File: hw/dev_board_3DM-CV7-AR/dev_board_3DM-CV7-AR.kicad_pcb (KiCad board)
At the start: 2 copper layers, 66.5 x 35 mm, 11 parts

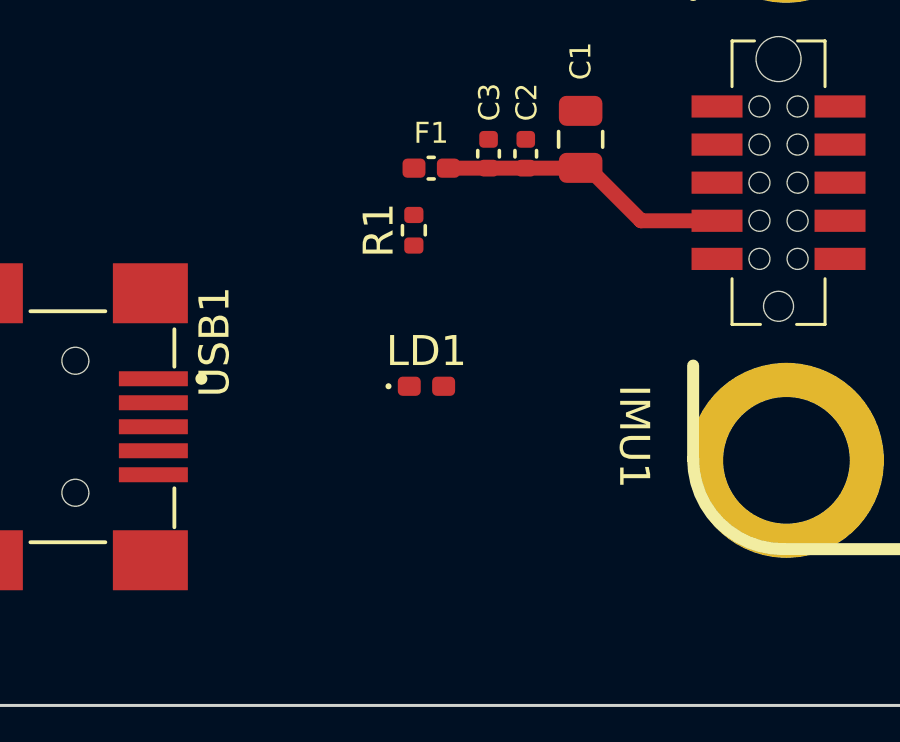
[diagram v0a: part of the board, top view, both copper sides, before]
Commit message: Añadido CM Choke
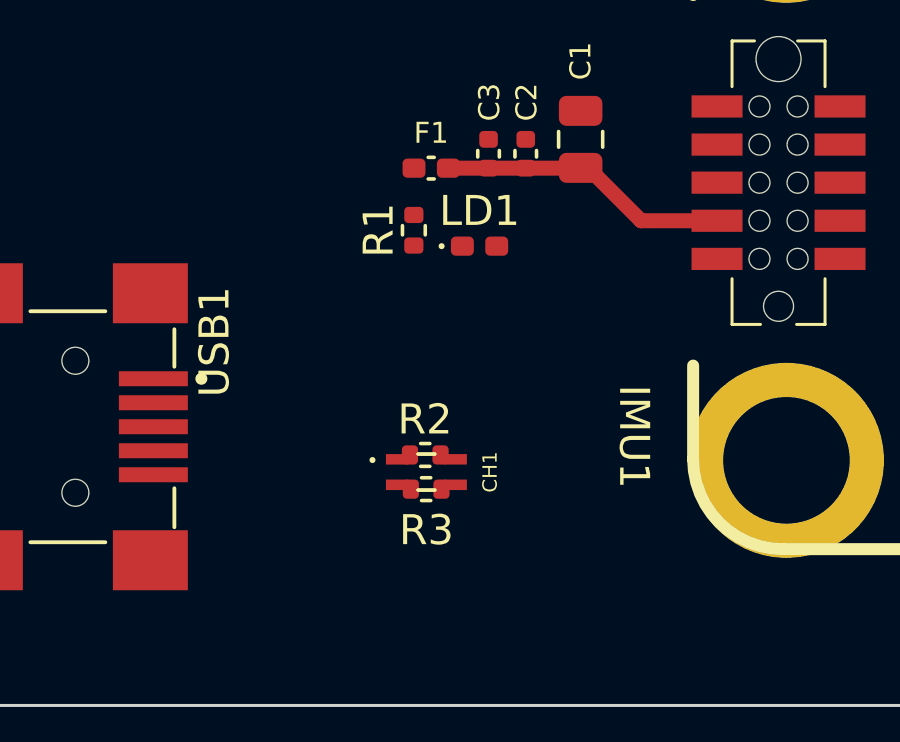
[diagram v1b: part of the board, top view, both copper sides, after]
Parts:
- added CH1: ~, Herranz - Filtering:XFMR_CM0805D900R-10, F.Cu at (111.0, 106.9)
- added R2: 0, Resistor_SMD:R_0402_1005Metric, F.Cu at (111.0, 106.4)
- added R3: 0, Resistor_SMD:R_0402_1005Metric, F.Cu at (111.0, 107.5)
- moved LD1 4.99 mm to (112.8, 99.4)
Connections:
- IMU1 pad 1: unconnected-(IMU1-USB_D--Pad1) -> Net-(IMU1-USB_D-)
- IMU1 pad 2: unconnected-(IMU1-USB_D+-Pad2) -> Net-(IMU1-USB_D+)
- USB1 pad 2: unconnected-(USB1-D--Pad2) -> Net-(USB1-D-)
- USB1 pad 3: unconnected-(USB1-D+-Pad3) -> Net-(USB1-D+)

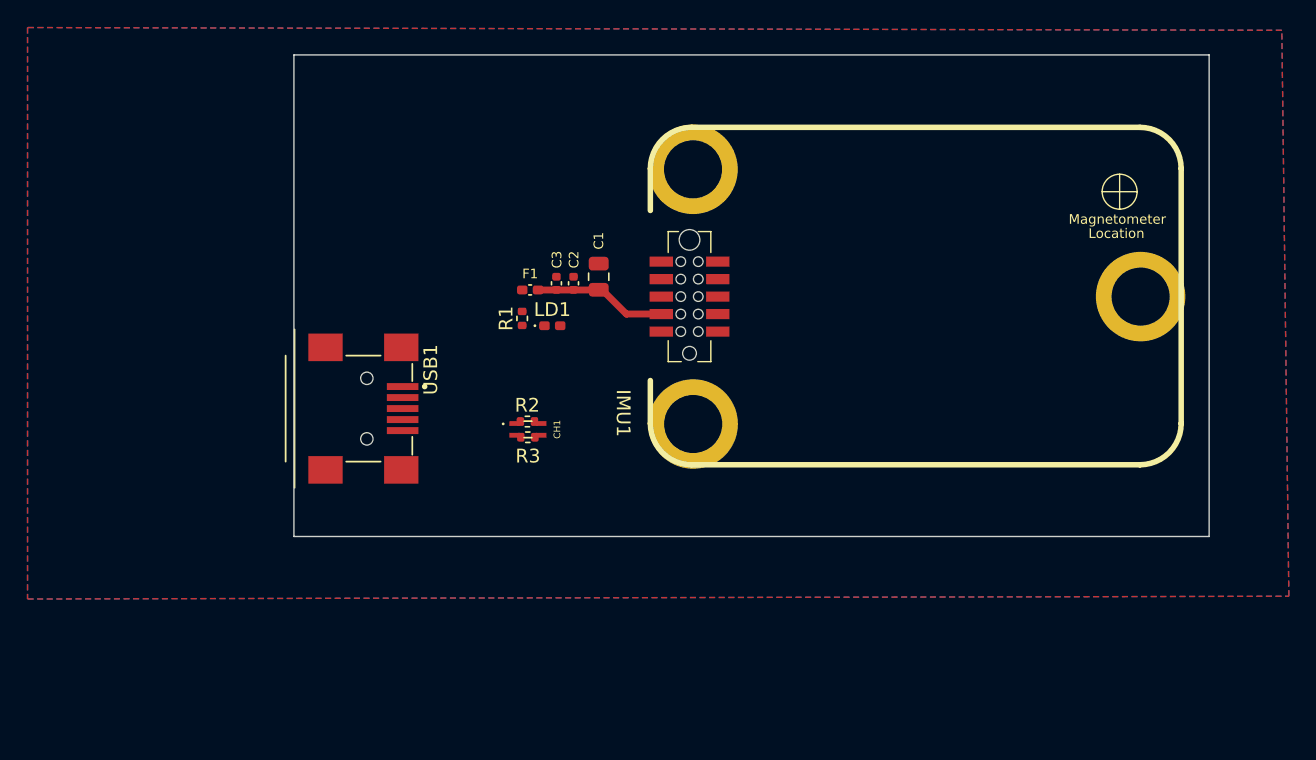
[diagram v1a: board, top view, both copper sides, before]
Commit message: Añadido Leds TX-RX
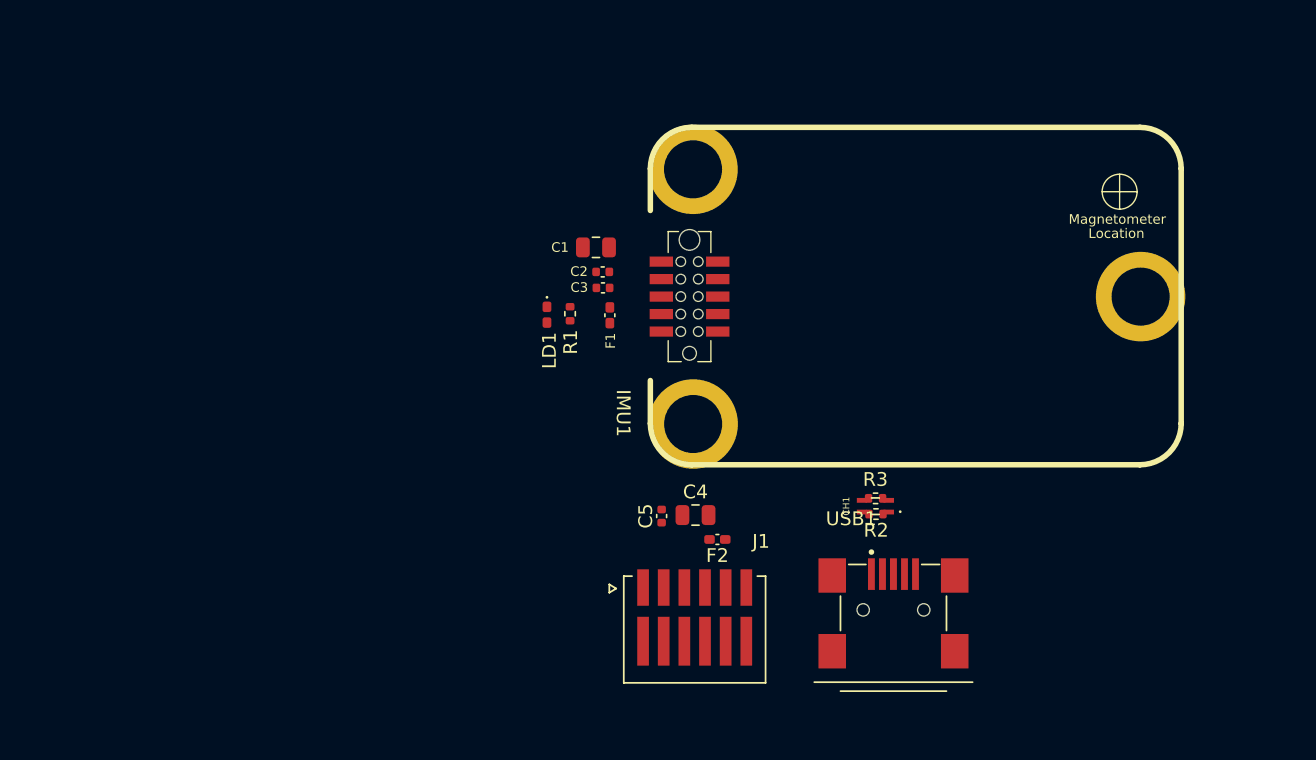
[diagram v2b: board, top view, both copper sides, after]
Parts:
- added C4: 0.1uF, Capacitor_SMD:C_0805_2012Metric, F.Cu at (123.2, 113.2)
- added C5: 0.1uF, Capacitor_SMD:C_0402_1005Metric, F.Cu at (120.7, 113.2)
- added F2: ~, Inductor_SMD:L_0402_1005Metric_Pad0.77x0.64mm_HandSolder, F.Cu at (124.8, 114.9)
- added J1: 87438-0643, Herranz - Conn Molex:Molex_picoSPOX_87438-3.5A_1x6_P1.5mm_Horizontal, F.Cu at (123.2, 113.2)
- moved USB1 37.8 mm to (137.6, 117.6), turned to 0 degrees
- moved R2 26.2 mm to (136.3, 113.1), turned to 180 degrees
- moved CH1 25.8 mm to (136.2, 112.5), turned to 180 degrees
- moved R3 25.6 mm to (136.2, 112.0), turned to 180 degrees
- moved F1 6.08 mm to (117.0, 98.7), turned to 90 degrees
- moved R1 3.50 mm to (114.1, 98.5), turned to -90 degrees
- moved C3 3.40 mm to (116.5, 96.7), turned to 180 degrees
- moved C2 2.28 mm to (116.4, 95.5), turned to 180 degrees
- moved C1 2.14 mm to (115.9, 93.7), turned to 180 degrees
- moved LD1 0.89 mm to (112.4, 98.6), turned to -90 degrees
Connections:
- IMU1 pad 4: unconnected-(IMU1-RxD-Pad4) -> /Rx
- IMU1 pad 5: unconnected-(IMU1-TxD-Pad5) -> /Tx
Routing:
- net Net-(IMU1-VCC): track 9.69 -> 0.00 mm
- removed copper zone on B.Cu, net GND
- removed copper zone on F.Cu, net GND
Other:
- board outline removed

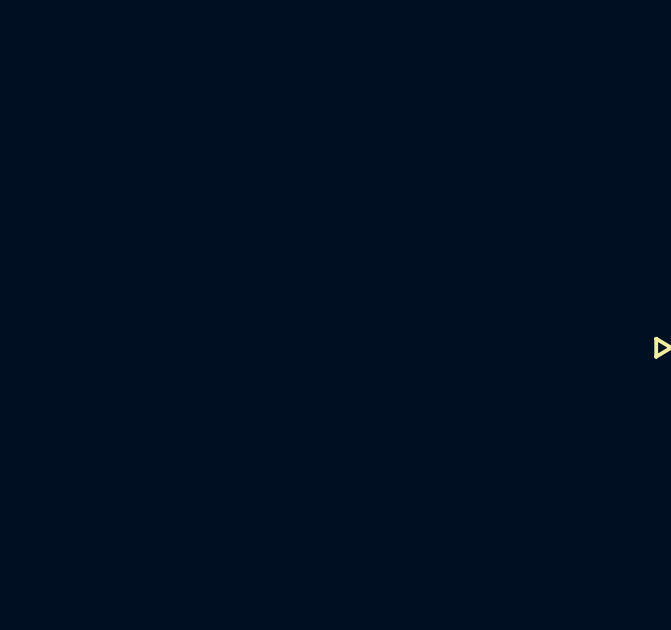
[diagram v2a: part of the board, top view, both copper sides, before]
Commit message: arreglado linea diferencial
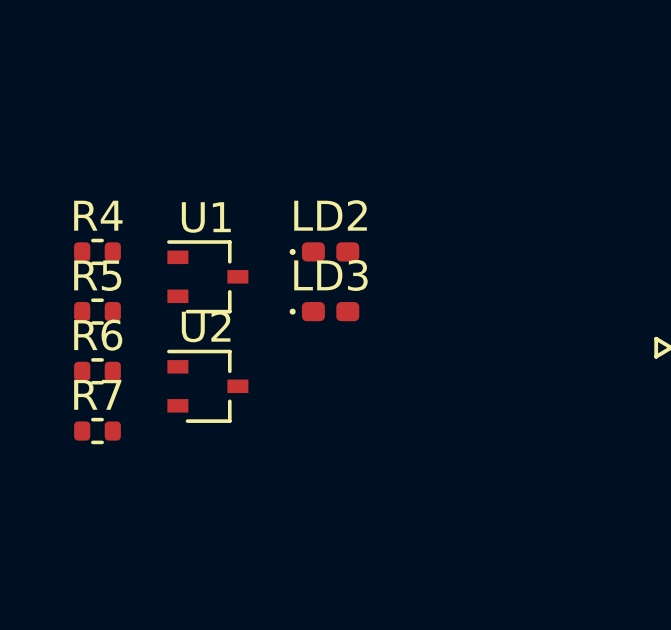
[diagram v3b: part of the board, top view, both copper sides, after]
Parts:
- added LD2: LED_Generic, LED_SMD:LED_0402_1005Metric_Pad0.77x0.64mm_HandSolder, F.Cu at (106.1, 115.3)
- added LD3: LED_Generic, LED_SMD:LED_0402_1005Metric_Pad0.77x0.64mm_HandSolder, F.Cu at (106.1, 117.3)
- added R4: 0, Resistor_SMD:R_0402_1005Metric, F.Cu at (98.3, 115.3)
- added R5: 0, Resistor_SMD:R_0402_1005Metric, F.Cu at (98.3, 117.3)
- added R6: 1.0K, Resistor_SMD:R_0402_1005Metric, F.Cu at (98.3, 119.3)
- added R7: 1.0K, Resistor_SMD:R_0402_1005Metric, F.Cu at (98.3, 121.3)
- added U1: DMP2240UW, Package_TO_SOT_SMD:SOT-323_SC-70, F.Cu at (102.0, 116.1)
- added U2: DMP2240UW, Package_TO_SOT_SMD:SOT-323_SC-70, F.Cu at (102.0, 119.8)
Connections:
- net Net-(IMU1-USB_D+) renamed /D+
- net Net-(IMU1-USB_D-) renamed /D-
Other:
- copper layers 2 -> 4

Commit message: Finalizado
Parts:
- added MC4: M3_Hole, Herranz - Various:M3_Hole, F.Cu at (157.4, 122.0)
- added MC5: M3_Hole, Herranz - Various:M3_Hole, F.Cu at (114.4, 86.7)
- added MC6: M3_Hole, Herranz - Various:M3_Hole, F.Cu at (114.4, 122.0)
- added SEL1: ~, Herranz - Various:pad_selector, F.Cu at (120.3, 113.2)
- moved R6 18.9 mm to (113.3, 107.8)
- moved R7 17.7 mm to (113.1, 111.7)
- moved R5 17.6 mm to (115.7, 115.2), turned to 180 degrees
- moved R4 16.0 mm to (113.3, 109.8)
- moved U1 15.7 mm to (115.9, 108.8), turned to 90 degrees
- moved U2 15.6 mm to (115.9, 112.7), turned to 90 degrees
- moved LD2 11.6 mm to (113.4, 106.3)
- moved LD3 8.12 mm to (113.2, 113.4)
- moved C4 2.78 mm to (125.9, 113.2)
- moved C5 2.78 mm to (123.5, 113.2)
- moved F2 2.78 mm to (127.5, 114.9)
- moved J1 2.78 mm to (125.9, 113.2)
- moved USB1 1.95 mm to (139.5, 117.6)
- moved CH1 1.95 mm to (138.2, 112.5)
- moved R2 1.95 mm to (138.2, 113.0)
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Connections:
- net Net-(USB1-D+) renamed /D_conn+
- net Net-(USB1-D-) renamed /D_conn-
- F1 pad 1: +3V3 -> +5VD
- MC3 pad 1: GND -> unconnected-(MC3-Pad1)
- R1 pad 2: +3V3 -> +5VD
- R6 pad 2: Net-(U1-S) -> Net-(U1-D)
- R7 pad 2: Net-(U2-S) -> Net-(U2-D)
- U1 pad 2: Net-(U1-S) -> +5VD
- U1 pad 3: +3V3 -> Net-(U1-D)
- U2 pad 2: Net-(U2-S) -> +5VD
- U2 pad 3: +3V3 -> Net-(U2-D)
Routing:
- net /Rx: track 0.00 -> 48.2 mm, vias 0 -> 2
- net /Tx: track 0.00 -> 35.9 mm, vias 0 -> 3
- net /D-: track 0.00 -> 24.0 mm
- net +5VD: track 0.00 -> 22.0 mm
- net VBUS: track 0.00 -> 21.0 mm
- net /D+: track 0.00 -> 19.3 mm
- net +5V: track 0.00 -> 8.59 mm
- net Net-(IMU1-VCC): track 0.00 -> 8.32 mm
- net /D_conn+: track 0.00 -> 7.97 mm
- net /D_conn-: track 0.00 -> 7.31 mm
- net Net-(J1-Pin_5): track 0.00 -> 3.50 mm
- net Net-(U2-D): track 0.00 -> 2.23 mm
- net Net-(U1-D): track 0.00 -> 2.06 mm
- net Net-(LD3-A): track 0.00 -> 1.75 mm
- net Net-(LD1-A): track 0.00 -> 1.68 mm
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- added copper zone on B.Cu, net GND
- added copper zone on F.Cu, net GND
- added copper zone on In1.Cu, net GND
- added copper zone on In2.Cu, net GND
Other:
- board outline added: 49.7 x 42 mm
